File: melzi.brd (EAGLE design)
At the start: 208.3 x 49.5 mm, 121 parts, among them IC5 7805DT, IC6 ATMEGA1284P, IC7 4050D, IC8 FT232RL-BASICSSOP, M1 RFP30N06LE, M2 RFP30N06LE, M3 RFP30N06LE, Q1 16MHZ, U1 A4982, U2 A4982, U3 A4982, U4 A4982, X1 MICROSD, X2 MINI-USB-SHIELD-UX60-MB-5ST

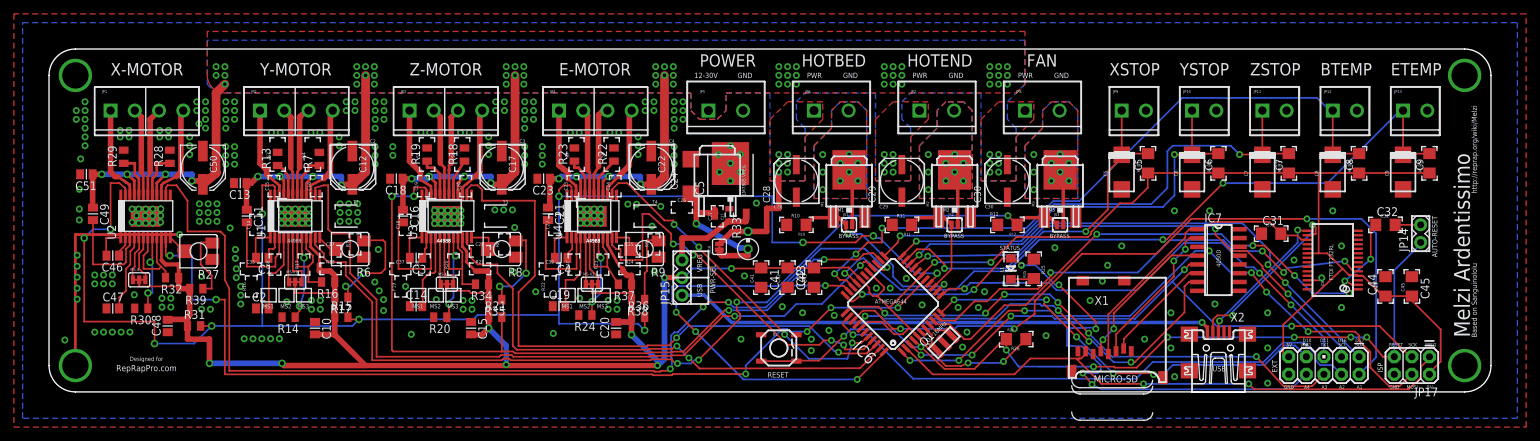
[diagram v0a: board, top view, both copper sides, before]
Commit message: Extensive rerouting to give 10 thou clearance between tracks.
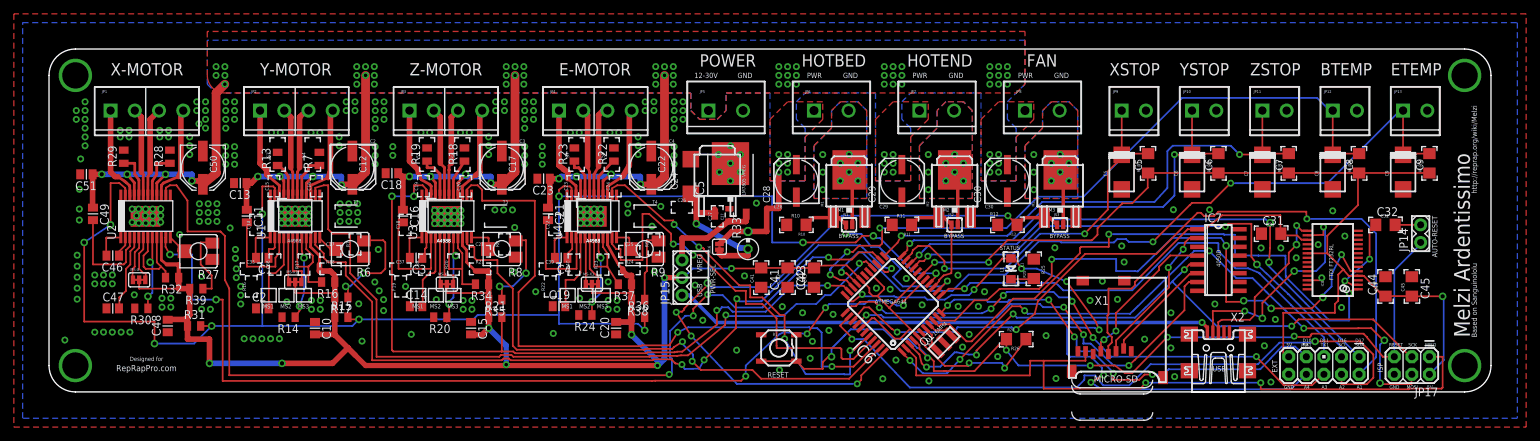
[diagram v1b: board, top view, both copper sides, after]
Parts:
- moved C18 1.02 mm to (49.5, 31.6)
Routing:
- net GND: track 36.4 -> 2.42 mm, vias 308 -> 324
- net MISO: track 85.2 -> 102.0 mm
- net EXT-A2: track 81.3 -> 97.8 mm, vias 1 -> 2
- net AOFI: track 69.2 -> 85.5 mm, vias 4 -> 6
- net VCC: track 444.5 -> 456.0 mm, vias 12 -> 13
- net AIFO: track 72.5 -> 83.6 mm, vias 4 -> 2
- net USBDM: track 25.5 -> 32.8 mm, vias 2 -> 4
- net !RESET: track 123.1 -> 129.9 mm, vias 8 -> 6
- net E-DIR: track 51.2 -> 57.7 mm
- net MOSI: track 94.1 -> 99.1 mm
- net VDD: track 41.5 -> 46.2 mm
- net E-STEP: track 57.4 -> 62.0 mm, vias 4 -> 2
- net Z-DIR: track 89.9 -> 94.3 mm
- net SCLK: track 87.0 -> 90.6 mm
- net X-DIR: track 140.6 -> 144.1 mm
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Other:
- board text added: "reprappro.com RepRap Melzi V2.0 Licence: GPL Design: Joe Mosfet & Adrian"
- board text removed: "reprappro.com RepRap Melzi V2.0 Licence: GPL"
